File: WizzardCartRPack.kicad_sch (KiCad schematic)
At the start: 7 parts, among them SW1 SW_DIP_x05, U1 27C801

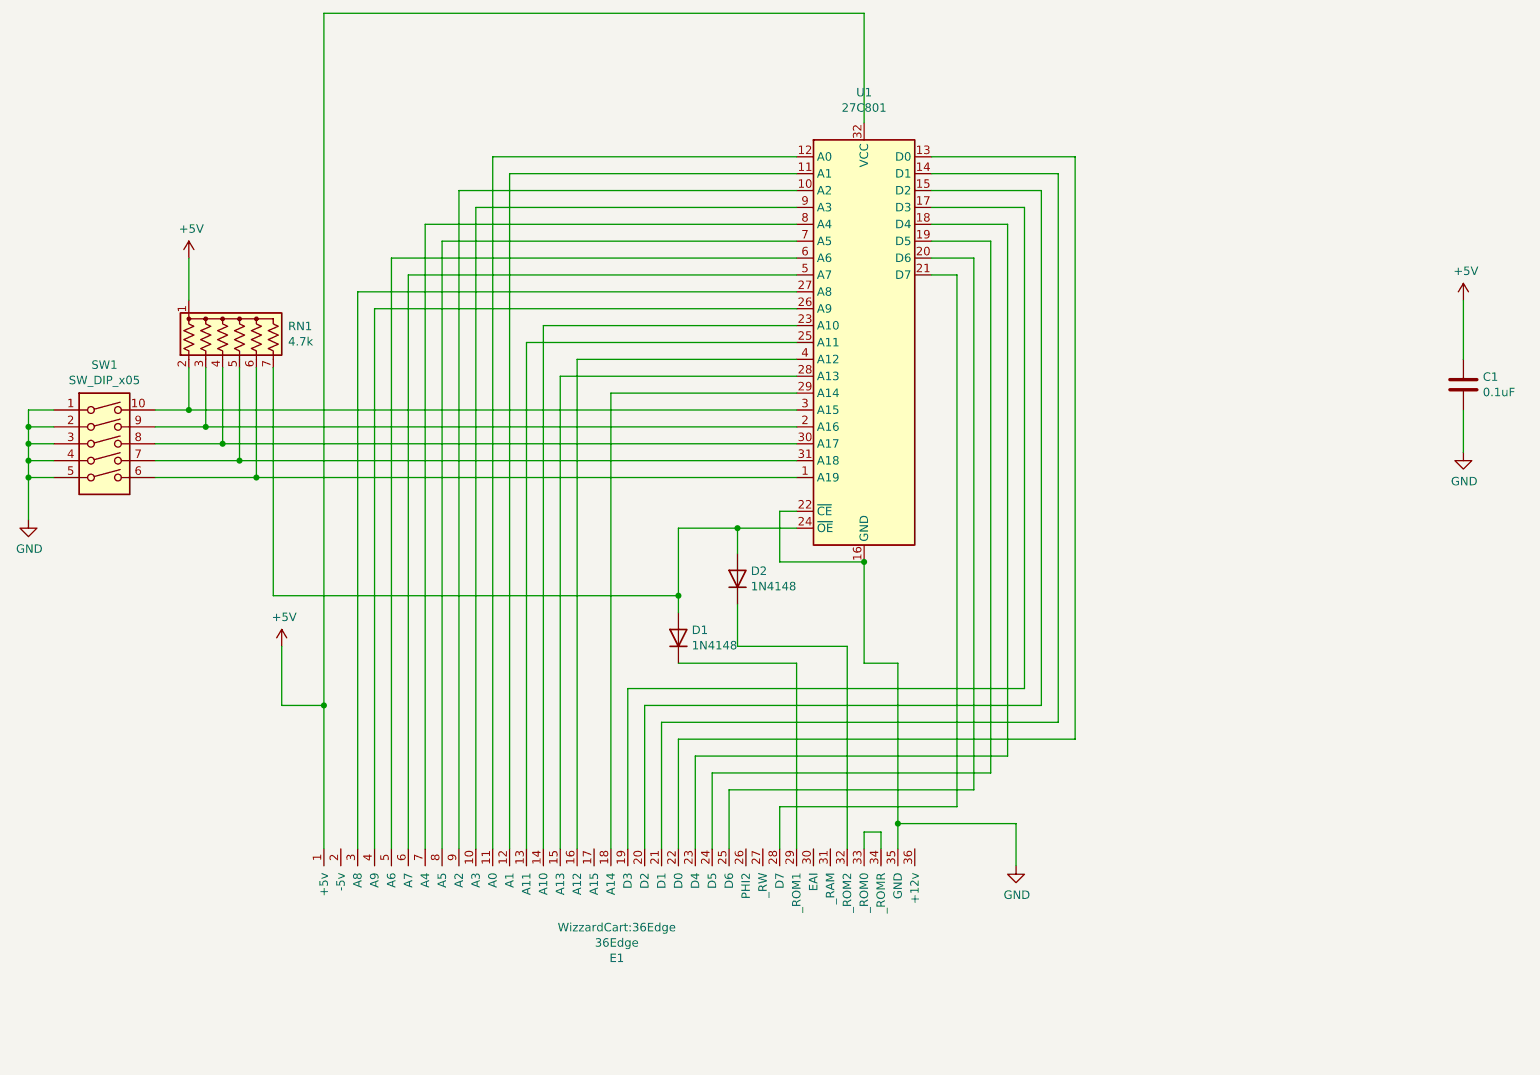
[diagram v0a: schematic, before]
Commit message: Fabricated single-ROM version
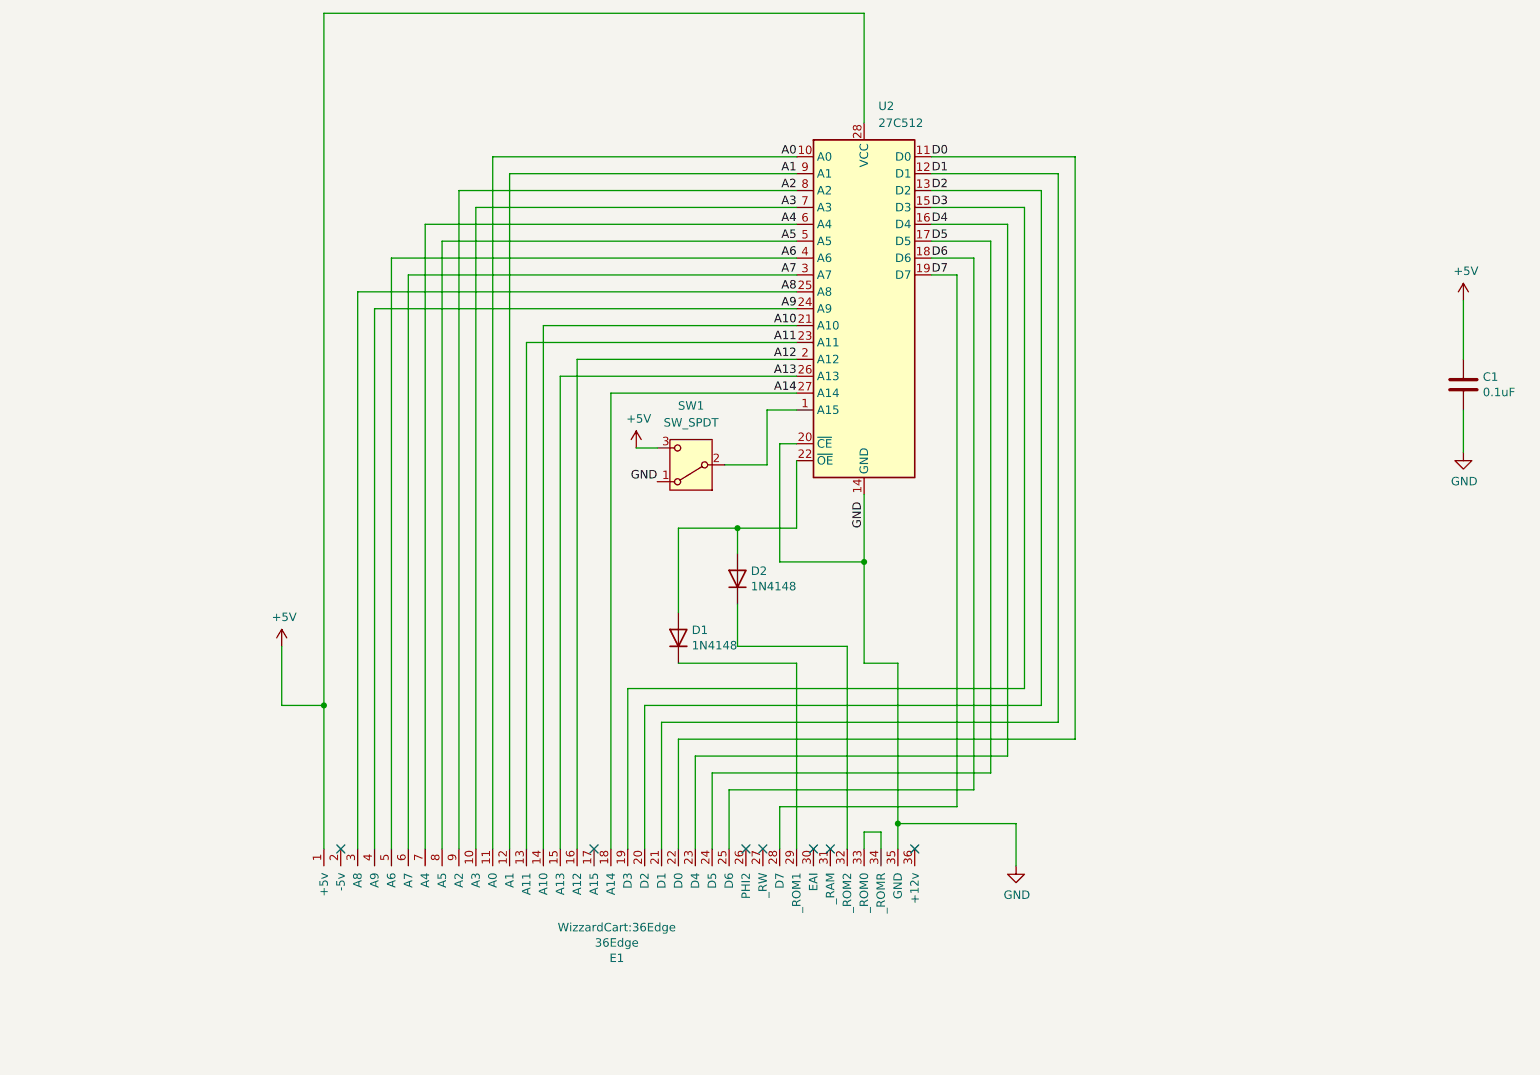
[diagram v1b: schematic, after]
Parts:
- removed RN1: 4.7k, Resistor_THT:R_Array_SIP7, symbol Device:R_Network06_US
- removed SW1: SW_DIP_x05, Package_DIP:DIP-10_W7.62mm_Socket_LongPads, symbol Switch:SW_DIP_x05
- removed U1: 27C801, Package_DIP:DIP-32_W15.24mm_Socket_LongPads, symbol Memory_EPROM:27C080
- added SW1: SW_SPDT, Connector_PinHeader_2.54mm:PinHeader_1x03_P2.54mm_Vertical, symbol Switch:SW_SPDT
- added U2: 27C512, Package_DIP:DIP-28_W15.24mm, symbol Memory_EPROM:27C512
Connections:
- net +5V: now also SW1.3 (C), U2.28 (VCC)
- net GND: now also SW1.1 (A), U2.14 (GND), U2.20 (~{CE})
- net A3: now reaches E1.10 (A3)
- net A3: now also U2.7 (A3)
- net A0: now reaches E1.11 (A0)
- net A0: now also U2.10 (A0)
- net A1: now reaches E1.12 (A1)
- net A1: now also U2.9 (A1)
- net A11: now reaches E1.13 (A11)
- net A11: now also U2.23 (A11)
- net A10: now reaches E1.14 (A10)
- net A10: now also U2.21 (A10)
- net A13: now reaches E1.15 (A13)
- net A13: now also U2.26 (A13)
- net A12: now reaches E1.16 (A12)
- net A12: now also U2.2 (A12)
- net A14: now reaches E1.18 (A14)
- net A14: now also U2.27 (A14)
- net D3: now reaches E1.19 (D3)
- net D3: now also U2.15 (D3)
- net D2: now reaches E1.20 (D2)
- net D2: now also U2.13 (D2)
- net D1: now reaches E1.21 (D1)
- net D1: now also U2.12 (D1)
- net D0: now reaches E1.22 (D0)
- net D0: now also U2.11 (D0)
- net D4: now reaches E1.23 (D4)
- net D4: now also U2.16 (D4)
- net D5: now reaches E1.24 (D5)
- net D5: now also U2.17 (D5)
- net D6: now reaches E1.25 (D6)
- net D6: now also U2.18 (D6)
- net D7: now reaches E1.28 (D7)
- net D7: now also U2.19 (D7)
- net A8: now reaches E1.3 (A8)
- net A8: now also U2.25 (A8)
- net A9: now reaches E1.4 (A9)
- net A9: now also U2.24 (A9)
- net A6: now reaches E1.5 (A6)
- net A6: now also U2.4 (A6)
- net A7: now reaches E1.6 (A7)
- net A7: now also U2.3 (A7)
- net A4: now reaches E1.7 (A4)
- net A4: now also U2.6 (A4)
- net A5: now reaches E1.8 (A5)
- net A5: now also U2.5 (A5)
- net A2: now reaches E1.9 (A2)
- net A2: now also U2.8 (A2)
- net at D1.2 (A), D2.2 (A): now also U2.22 (~{OE})
- new net: SW1.2 (B), U2.1 (A15)
- no-connect marks 0 -> 7

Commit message: Move fingers up
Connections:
- net ~{ROM1}: now reaches D1.1 (K), E1.29 (_ROM1)
- net ~{ROM2}: now reaches D2.1 (K), E1.32 (_ROM2)
- net ~{OE}: now reaches D1.2 (A), D2.2 (A), U2.22 (~{OE})
- net A15: now reaches SW1.2 (B), U2.1 (A15)
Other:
- note added: "Always decode BIOS"
- moved on the sheet: D1
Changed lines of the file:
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@@
 	(generator_version "9.0")
 	(paper "A4")
+	(text "Always decode BIOS"
+		(exclude_from_sim no)
+		(at 149.225 173.355 90)
+		(effects
+			(font
+				(size 1.27 1.27)
+			)
+		)
+	)
 	(junction
 		(at 66.04 130.81)
@@
 		)
 	)
+	(label "A15"
+		(at 133.35 86.36 0)
+		(effects
+			(font
+				(size 1.27 1.27)
+			)
+			(justify left bottom)
+		)
+	)
 	(label "D2"
 		(at 157.48 53.34 0)
@@
 		)
 	)
+	(label "~{ROM2}"
+		(at 132.08 121.92 0)
+		(effects
+			(font
+				(size 1.27 1.27)
+			)
+			(justify left bottom)
+		)
+	)
 	(label "A8"
 		(at 137.16 68.58 180)
@@
 		)
 	)
+	(label "~{OE}"
+		(at 130.175 104.14 0)
+		(effects
+			(font
+				(size 1.27 1.27)
+			)
+			(justify left bottom)
+		)
+	)
 	(label "D5"
 		(at 157.48 60.96 0)
@@
 	(label "D7"
 		(at 157.48 66.04 0)
+		(effects
+			(font
+				(size 1.27 1.27)
+			)
+			(justify left bottom)
+		)
+	)
+	(label "~{ROM1}"
+		(at 132.08 124.46 0)
 		(effects
 			(font
@@
 	(symbol
 		(lib_id "Diode:1N4148")
-		(at 119.38 120.65 90)
+		(at 119.38 120.65 270)
+		(mirror x)
 		(unit 1)
 		(exclude_from_sim no)
@@
 		(dnp no)
 		(property "Reference" "D1"
-			(at 121.3866 119.4816 90)
+			(at 117.3734 119.4816 90)
 			(effects
 				(font
@@
 		)
 		(property "Value" "1N4148"
-			(at 121.3866 121.793 90)
+			(at 117.3734 121.793 90)
 			(effects
 				(font
@@
 		)
 		(property "Footprint" "Diode_THT:D_DO-35_SOD27_P7.62mm_Horizontal"
-			(at 123.825 120.65 0)
+			(at 114.935 120.65 0)
 			(effects
 				(font
